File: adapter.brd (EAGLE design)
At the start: 15.3 x 34.7 mm, 14 parts, among them J1 71607-313LF

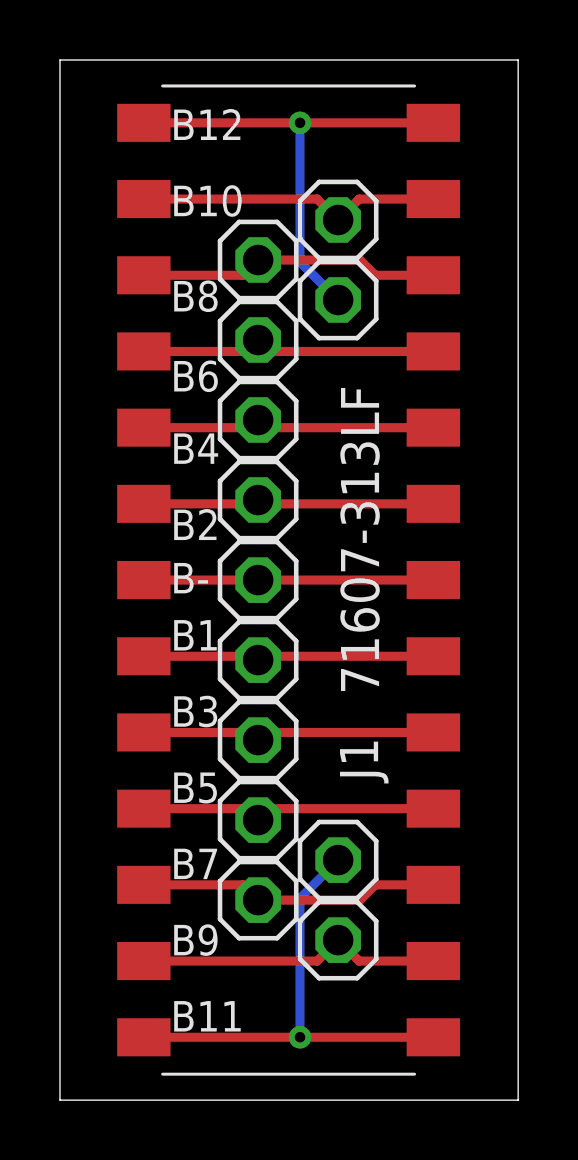
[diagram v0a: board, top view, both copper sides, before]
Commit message: minimize pcb size
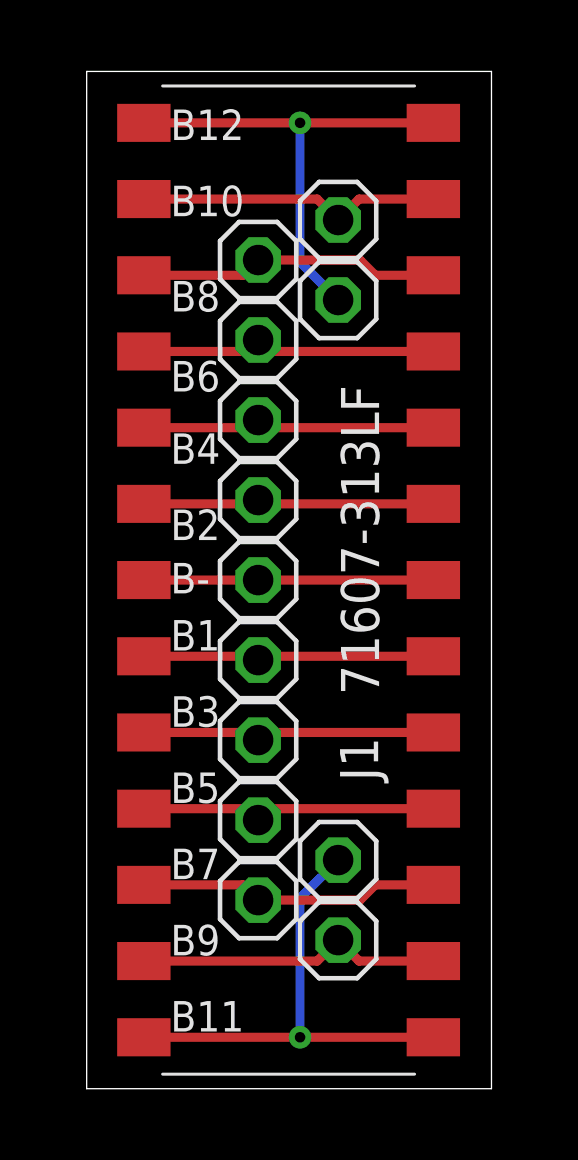
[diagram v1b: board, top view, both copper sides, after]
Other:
- board size 15.3 x 34.7 mm -> 13.5 x 33.9 mm
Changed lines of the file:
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@@
 <board>
 <plain>
-<wire x1="0" y1="0" x2="15.27175" y2="0" width="0" layer="20"/>
-<wire x1="15.27175" y1="0" x2="15.27175" y2="34.671" width="0" layer="20"/>
-<wire x1="15.27175" y1="34.671" x2="0" y2="34.671" width="0" layer="20"/>
-<wire x1="0" y1="34.671" x2="0" y2="0" width="0" layer="20"/>
+<wire x1="0.889" y1="0.381" x2="14.38275" y2="0.381" width="0" layer="20"/>
+<wire x1="14.38275" y1="0.381" x2="14.38275" y2="34.29" width="0" layer="20"/>
+<wire x1="14.38275" y1="34.29" x2="0.889" y2="34.29" width="0" layer="20"/>
+<wire x1="0.889" y1="34.29" x2="0.889" y2="0.381" width="0" layer="20"/>
 <dimension x1="15.27175" y1="34.671" x2="0" y2="34.671" x3="7.635875" y3="36.0045" textsize="1.778" layer="1" unit="inch"/>
 <text x="3.683" y="32.004" size="1.016" layer="25">B12</text>

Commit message: fix labels
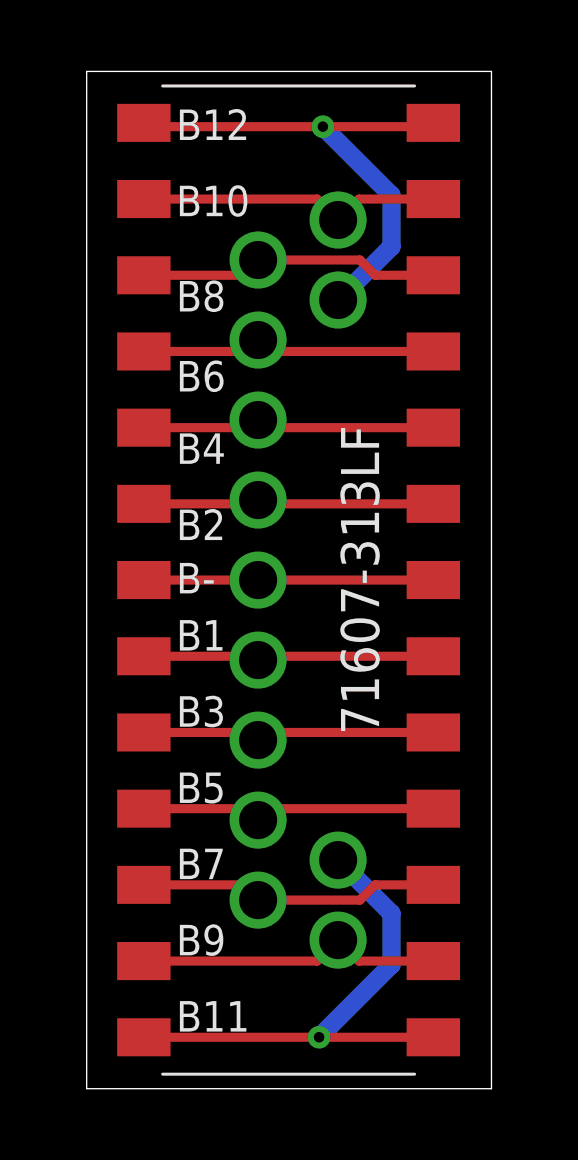
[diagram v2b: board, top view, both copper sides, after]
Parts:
- removed JP13, JP14: (no value), pinhead:1X01
- added JP-, JP1: (no value), ltobms:1X01BIG
- JP10, JP11, JP12, JP2, JP3, JP4, JP5, JP6, JP7, JP8, JP9: device pinhead:1X01 -> ltobms:1X01BIG
- moved JP11 17.5 mm to (9.27, 8.00)
- moved JP4 16.0 mm to (6.60, 22.7)
- moved JP9 14.9 mm to (9.27, 5.33)
- moved JP6 13.3 mm to (6.60, 25.3)
- moved JP2 12.3 mm to (6.60, 20.0)
- moved JP8 10.7 mm to (6.60, 28.0)
- moved JP7 8.00 mm to (6.60, 6.67)
- moved JP10 7.18 mm to (9.27, 29.3)
- moved JP3 7.18 mm to (6.60, 12.0)
- moved JP12 2.98 mm to (9.27, 26.7)
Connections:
- net B-: now also JP-.1; no longer JP8.1
- net B1: now also JP1.1; no longer JP7.1
- net B10: now also JP10.1; no longer JP13.1
- net B11: now also JP11.1; no longer JP2.1
- net B12: now also JP12.1; no longer JP14.1
- net B2: now also JP2.1; no longer JP9.1
- net B3: now also JP3.1; no longer JP6.1
- net B4: now also JP4.1; no longer JP10.1
- net B6: now also JP6.1; no longer JP11.1
- net B7: now also JP7.1; no longer JP4.1
- net B8: now also JP8.1; no longer JP12.1
- net B9: now also JP9.1; no longer JP3.1
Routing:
- net B11: track 16.1 -> 17.3 mm
- net B12: track 16.1 -> 17.2 mm

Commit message: add samtec footprint for more compatibility
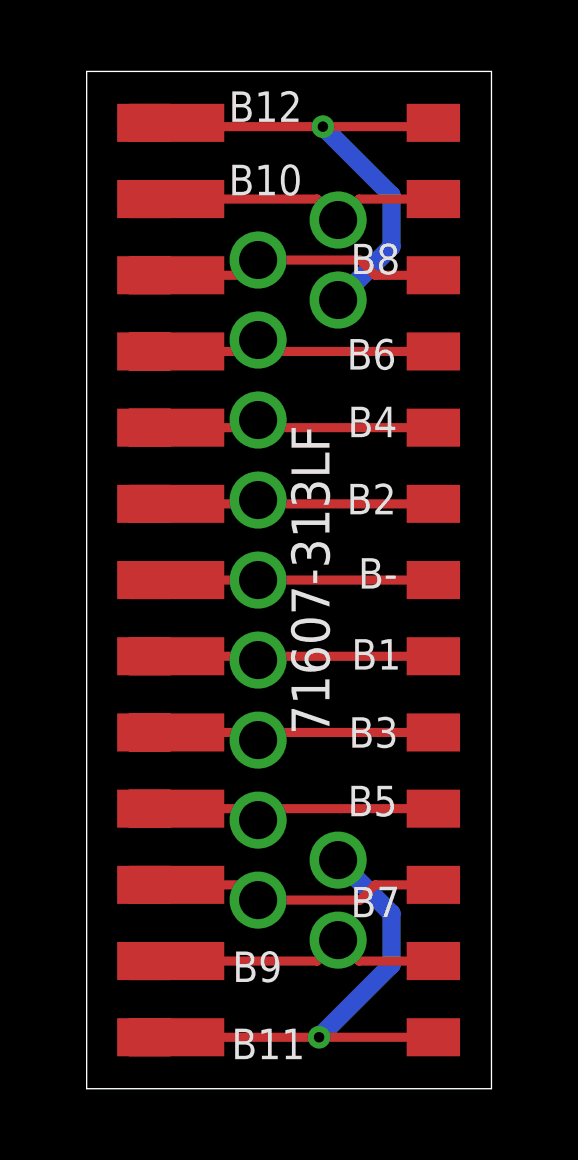
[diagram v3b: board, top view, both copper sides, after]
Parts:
- removed JP-: (no value), ltobms:1X01BIG
- added J2: TSM-113-01-L-SHJ, ltobms:TSM-113-01-L-SH
- added JP13: (no value), ltobms:1X01BIG
- moved JP10 24.0 mm to (9.27, 5.33)
- moved JP9 22.8 mm to (6.60, 28.0)
- moved JP11 21.3 mm to (9.27, 29.3)
- moved JP8 21.3 mm to (6.60, 6.67)
- moved JP12 18.7 mm to (9.27, 8.00)
- moved JP7 18.7 mm to (6.60, 25.3)
- moved JP6 16.0 mm to (6.60, 9.33)
- moved JP5 13.3 mm to (6.60, 22.7)
- moved JP4 10.7 mm to (6.60, 12.0)
- moved JP3 8.00 mm to (6.60, 20.0)
- moved JP2 5.33 mm to (6.60, 14.7)
- moved JP1 2.67 mm to (6.60, 17.3)
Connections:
- net B-: now also J2.7, JP1.1; no longer JP-.1
- net B1: now also J2.6, JP2.1; no longer JP1.1
- net B10: now also J2.12, JP11.1; no longer JP10.1
- net B11: now also J2.1, JP12.1; no longer JP11.1
- net B12: now also J2.13, JP13.1; no longer JP12.1
- net B2: now also J2.8, JP3.1; no longer JP2.1
- net B3: now also J2.5, JP4.1; no longer JP3.1
- net B4: now also J2.9, JP5.1; no longer JP4.1
- net B5: now also J2.4, JP6.1; no longer JP5.1
- net B6: now also J2.10, JP7.1; no longer JP6.1
- net B7: now also J2.3, JP8.1; no longer JP7.1
- net B8: now also J2.11, JP9.1; no longer JP8.1
- net B9: now also J2.2, JP10.1; no longer JP9.1
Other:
- board text added: "tinyurl.com/LTOBalance"
